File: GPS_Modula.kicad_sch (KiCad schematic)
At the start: 10 parts, among them U2 NEO-M8M, U5 AT24CS01-XHM

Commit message: fixed layout
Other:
- moved on the sheet: AE1
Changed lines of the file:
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@@
 	(wire
 		(pts
-			(xy 68.58 54.61) (xy 81.28 54.61)
+			(xy 68.58 54.61) (xy 77.47 54.61)
 		)
 		(stroke
@@
 	(wire
 		(pts
-			(xy 81.28 54.61) (xy 81.28 52.07)
+			(xy 77.47 54.61) (xy 77.47 52.07)
 		)
 		(stroke
@@
 	)
 	(global_label "Gps_V_Back"
-		(shape input)
+		(shape output)
 		(at 46.99 31.75 90)
 		(fields_autoplaced yes)
@@
 	(symbol
 		(lib_id "Device:Antenna")
-		(at 81.28 46.99 0)
+		(at 77.47 46.99 0)
 		(unit 1)
 		(exclude_from_sim no)
@@
 		(fields_autoplaced yes)
 		(property "Reference" "AE1"
-			(at 83.82 46.3549 0)
+			(at 80.01 46.3549 0)
 			(effects
 				(font
@@
 		)
 		(property "Value" "Antenna"
-			(at 83.82 48.8949 0)
+			(at 80.01 48.8949 0)
 			(effects
 				(font
@@
 		)
 		(property "Footprint" ""
-			(at 81.28 46.99 0)
+			(at 77.47 46.99 0)
 			(effects
 				(font
@@
 		)
 		(property "Datasheet" "~"
-			(at 81.28 46.99 0)
+			(at 77.47 46.99 0)
 			(effects
 				(font
@@
 		)
 		(property "Description" "Antenna"
-			(at 81.28 46.99 0)
-			(effects
-				(font
+			(at 77.47 46.99 0)
+			(effects
+				(font

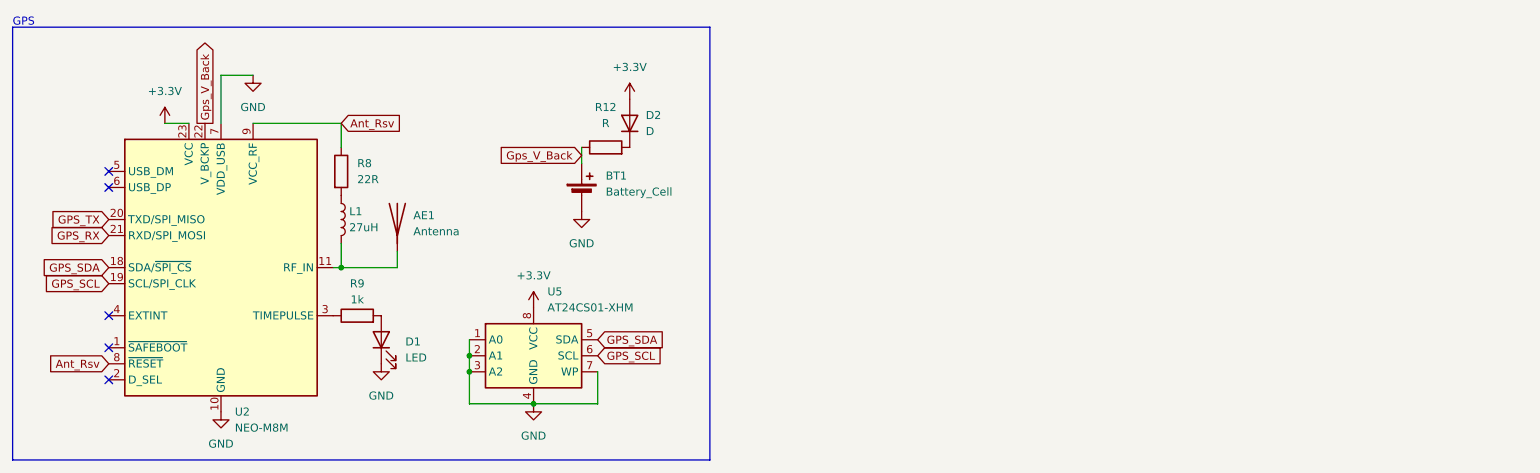
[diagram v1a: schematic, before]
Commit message: added psu and formated board outline
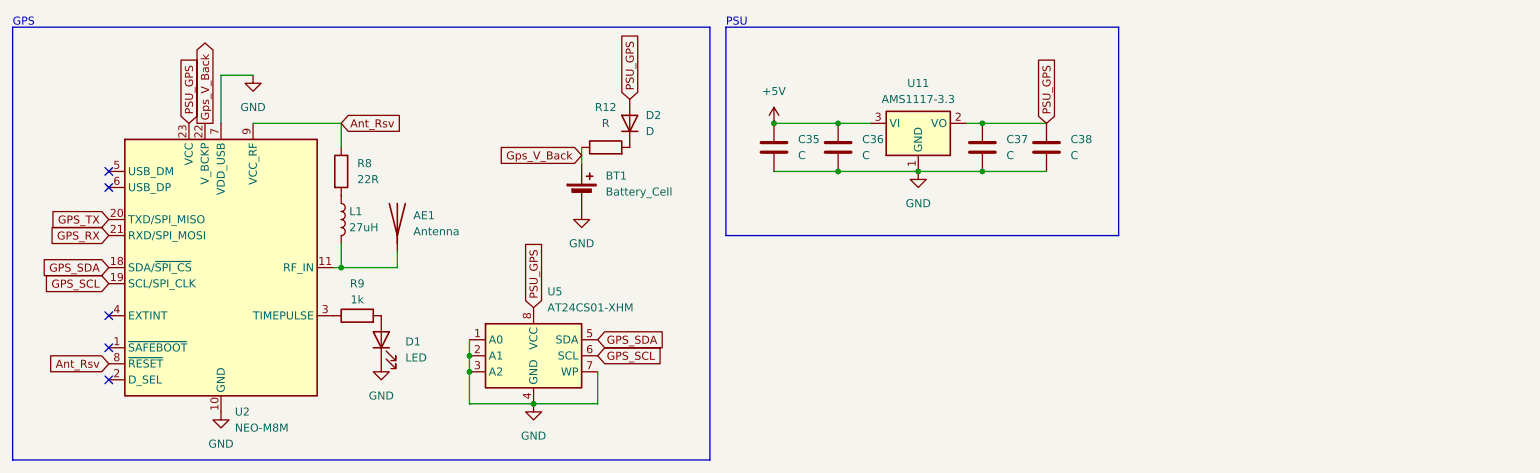
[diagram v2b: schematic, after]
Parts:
- added C35, C36, C37, C38: C, symbol Device:C
- added U11: AMS1117-3.3, Package_TO_SOT_SMD:SOT-223-3_TabPin2, symbol Regulator_Linear:AMS1117-3.3
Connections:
- net GND: now also C35.2, C36.2, C37.2, C38.2, U11.1 (GND)
- net +3.3V renamed PSU_GPS
- net PSU_GPS: now also C37.1, C38.1, U11.2 (VO)
- new net +5V: C35.1, C36.1, U11.3 (VI)
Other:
- note added: "PSU"

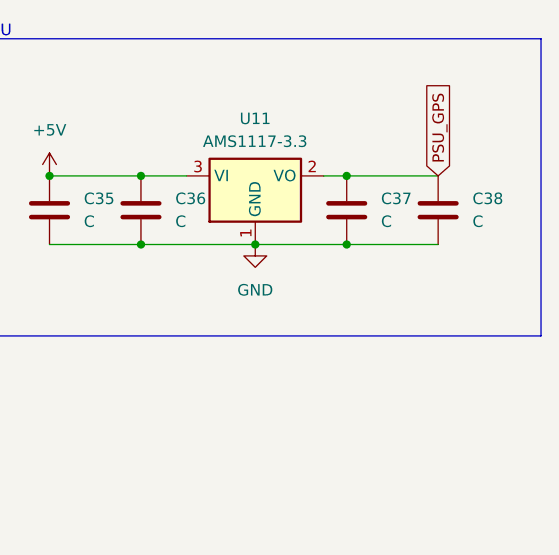
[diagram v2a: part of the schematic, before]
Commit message: added footprint for a7670e
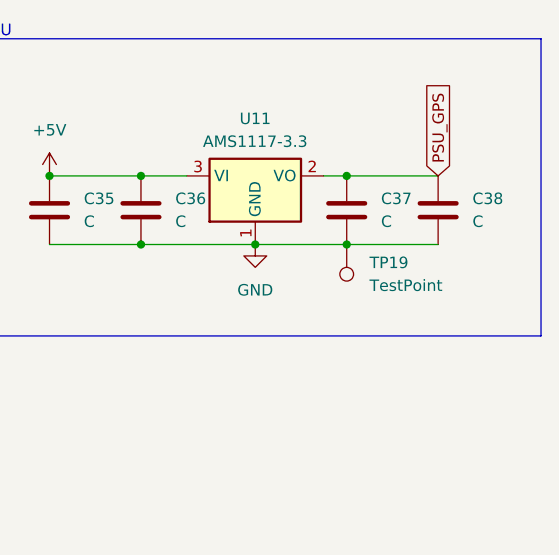
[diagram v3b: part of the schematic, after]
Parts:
- added TP19: TestPoint, symbol Connector:TestPoint
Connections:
- net GND: now also TP19.1
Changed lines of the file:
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@@
+	)
+	(symbol
+		(lib_id "Connector:TestPoint")
+		(at 170.18 39.37 180)
+		(unit 1)
+		(exclude_from_sim no)
+		(in_bom yes)
+		(on_board yes)
+		(dnp no)
+		(fields_autoplaced yes)
+		(property "Reference" "TP19"
+			(at 172.72 41.4019 0)
+			(effects
+				(font
+					(size 1.27 1.27)
+				)
+				(justify right)
+			)
+		)
+		(property "Value" "TestPoint"
+			(at 172.72 43.9419 0)
+			(effects
+				(font
+					(size 1.27 1.27)
+				)
+				(justify right)
+			)
+		)
+		(property "Footprint" ""
+			(at 165.1 39.37 0)
+			(effects
+				(font
+					(size 1.27 1.27)
+				)
+				(hide yes)
+			)
+		)
+		(property "Datasheet" "~"
+			(at 165.1 39.37 0)
+			(effects
+				(font
+					(size 1.27 1.27)
+				)
+				(hide yes)
+			)
+		)
+		(property "Description" "test point"
+			(at 170.18 39.37 0)
+			(effects
+				(font
+					(size 1.27 1.27)
+				)
+				(hide yes)
+			)
+		)
+		(pin "1"
+		)
+		(instances
+			(project "Hardware"
+				(path "/f04ee758-a926-48b7-b458-286a696c3ef4/645eb5eb-084e-44da-a26c-786606f44645"
+					(reference "TP19")
+					(unit 1)
+				)
+			)
+		)
 	)
 	(symbol

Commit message: done most of the schematics
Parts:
- removed AE1: Antenna, symbol Device:Antenna
- added J3: Conn_Coaxial, symbol Connector:Conn_Coaxial
- added TP3: TestPoint, symbol Connector:TestPoint
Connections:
- net GND: now also J3.2 (Ext)
- net Gps_V_Back: now also TP3.1
- net at L1.2, U2.11 (RF_IN): now also J3.1 (In)
- net PSU_GPS renamed PSU
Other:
- note added: "Battery"
- note added: "EEPROM"
- note added: "TODO"
- moved on the sheet: BT1, D1, D2, L1, R12, R8, R9, U2, U5

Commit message: done refacoring
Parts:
- removed D2: D, symbol Device:D
- added D2: 1N4148, Diode_THT:D_DO-35_SOD27_P7.62mm_Horizontal, symbol Diode:1N4148
- C35, C37: value C -> 10uF
- C36, C38: value C -> 100pF
- D1: footprint (none) -> Capacitor_SMD:C_0603_1608Metric
- J3: footprint (none) -> Connector_Coaxial:U.FL_Molex_MCRF_73412-0110_Vertical
- R12: value R -> 120R
- TP19, TP3: footprint (none) -> TestPoint:TestPoint_Pad_D2.5mm
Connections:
- net PSU: now also D2.2 (A)
- net at R12.2: now also D2.1 (K)
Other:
- note removed: "TODO"

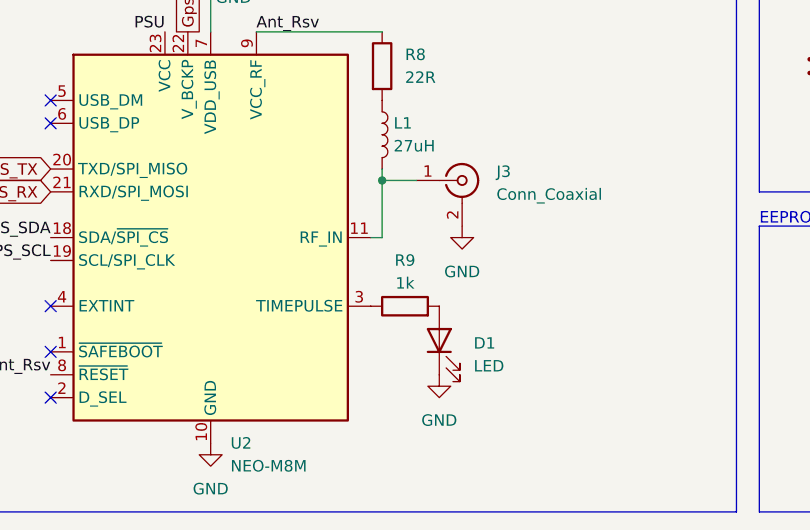
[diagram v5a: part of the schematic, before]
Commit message: assigned most footprints
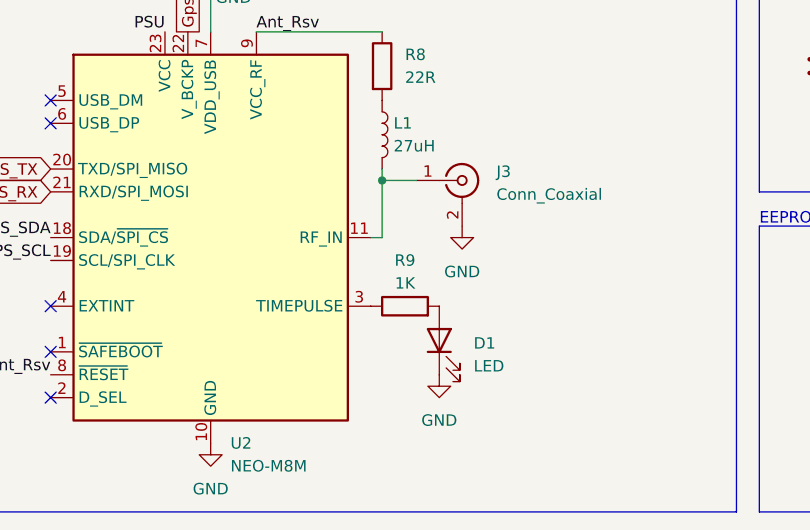
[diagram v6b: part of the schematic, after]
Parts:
- BT1: footprint (none) -> Battery:BatteryHolder_Seiko_MS621F
- L1: footprint (none) -> Inductor_SMD:L_0805_2012Metric
- R12, R8: footprint (none) -> Resistor_SMD:R_0603_1608Metric
- R9: value 1k -> 1K; footprint (none) -> Resistor_SMD:R_0603_1608Metric
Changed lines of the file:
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@@
 			)
 		)
-		(property "Footprint" ""
+		(property "Footprint" "Inductor_SMD:L_0805_2012Metric"
 			(at 87.63 43.18 0)
 			(effects
@@
 			)
 		)
-		(property "Value" "1k"
+		(property "Value" "1K"
 			(at 90.17 59.69 90)
 			(effects
@@
 			)
 		)
-		(property "Footprint" ""
+		(property "Footprint" "Resistor_SMD:R_0603_1608Metric"
 			(at 90.17 64.008 90)
 			(effects
@@
 			)
 		)
-		(property "Footprint" ""
+		(property "Footprint" "Resistor_SMD:R_0603_1608Metric"
 			(at 224.79 33.528 90)
 			(effects
@@
 			)
 		)
-		(property "Footprint" ""
+		(property "Footprint" "Battery:BatteryHolder_Seiko_MS621F"
 			(at 219.71 36.576 90)
 			(effects
@@
 			)
 		)
-		(property "Footprint" ""
+		(property "Footprint" "Resistor_SMD:R_0603_1608Metric"
 			(at 85.852 35.56 90)
 			(effects

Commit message: cleaned up scematics and updated power management
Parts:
- C35, C37: footprint (none) -> Capacitor_SMD:C_1206_3216Metric
- C36, C38: footprint (none) -> Capacitor_SMD:C_0805_2012Metric

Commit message: finelized scematics
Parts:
- TP19, TP3: footprint TestPoint:TestPoint_Pad_D2.5mm -> TestPoint:TestPoint_Pad_D2.0mm
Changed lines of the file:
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@@
 			)
 		)
-		(property "Footprint" "TestPoint:TestPoint_Pad_D2.5mm"
+		(property "Footprint" "TestPoint:TestPoint_Pad_D2.0mm"
 			(at 224.79 31.75 0)
 			(effects
@@
 			)
 		)
-		(property "Footprint" "TestPoint:TestPoint_Pad_D2.5mm"
+		(property "Footprint" "TestPoint:TestPoint_Pad_D2.0mm"
 			(at 165.1 39.37 0)
 			(effects
